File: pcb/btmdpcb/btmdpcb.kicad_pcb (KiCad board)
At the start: 2 copper layers, 60 x 25 mm, 34 parts, among them J2 ANT, T1 ED8_4, T2 ED8_4, U2 Pololu_U1V11F3, U3 LMV331

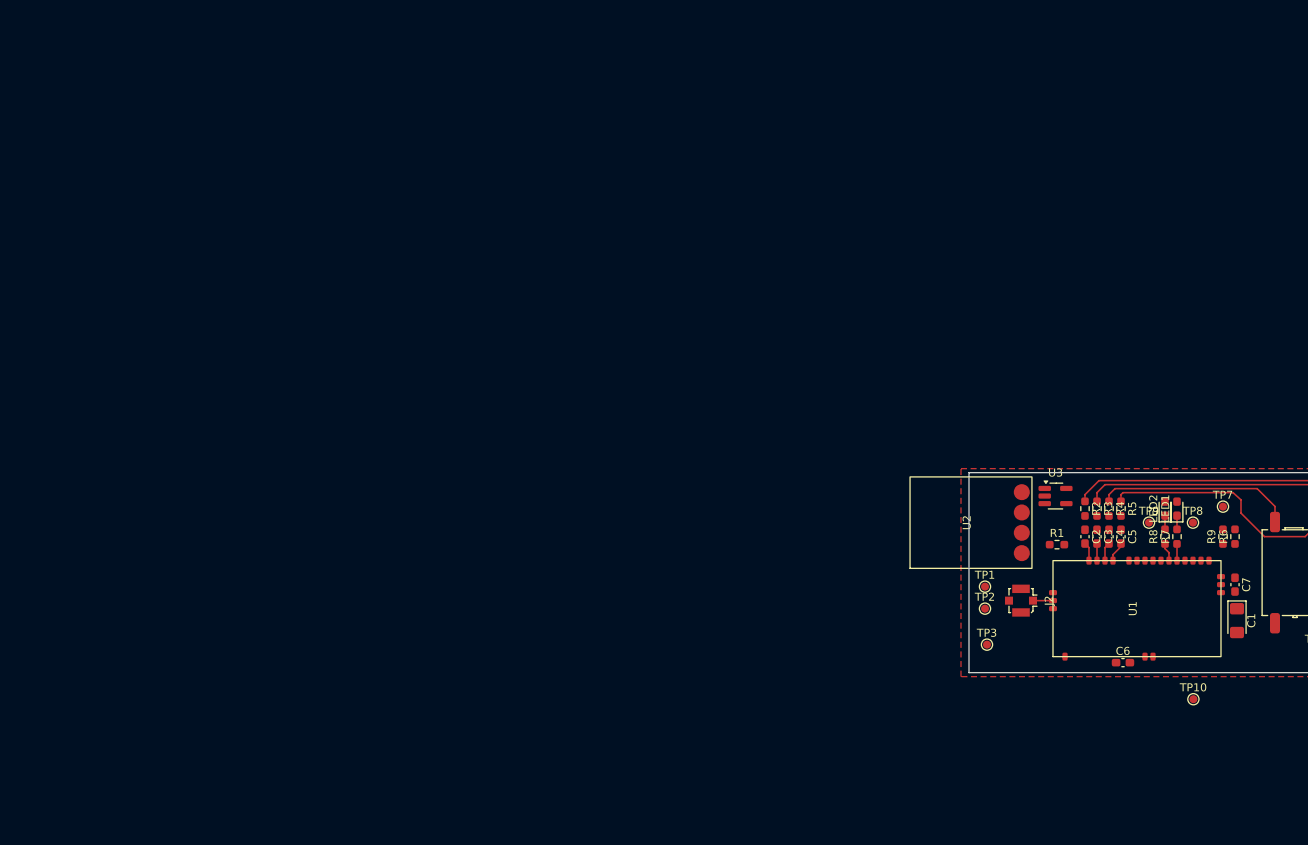
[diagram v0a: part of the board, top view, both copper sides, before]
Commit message: Update BT module symbol+footprint (correct power labels, add CE)
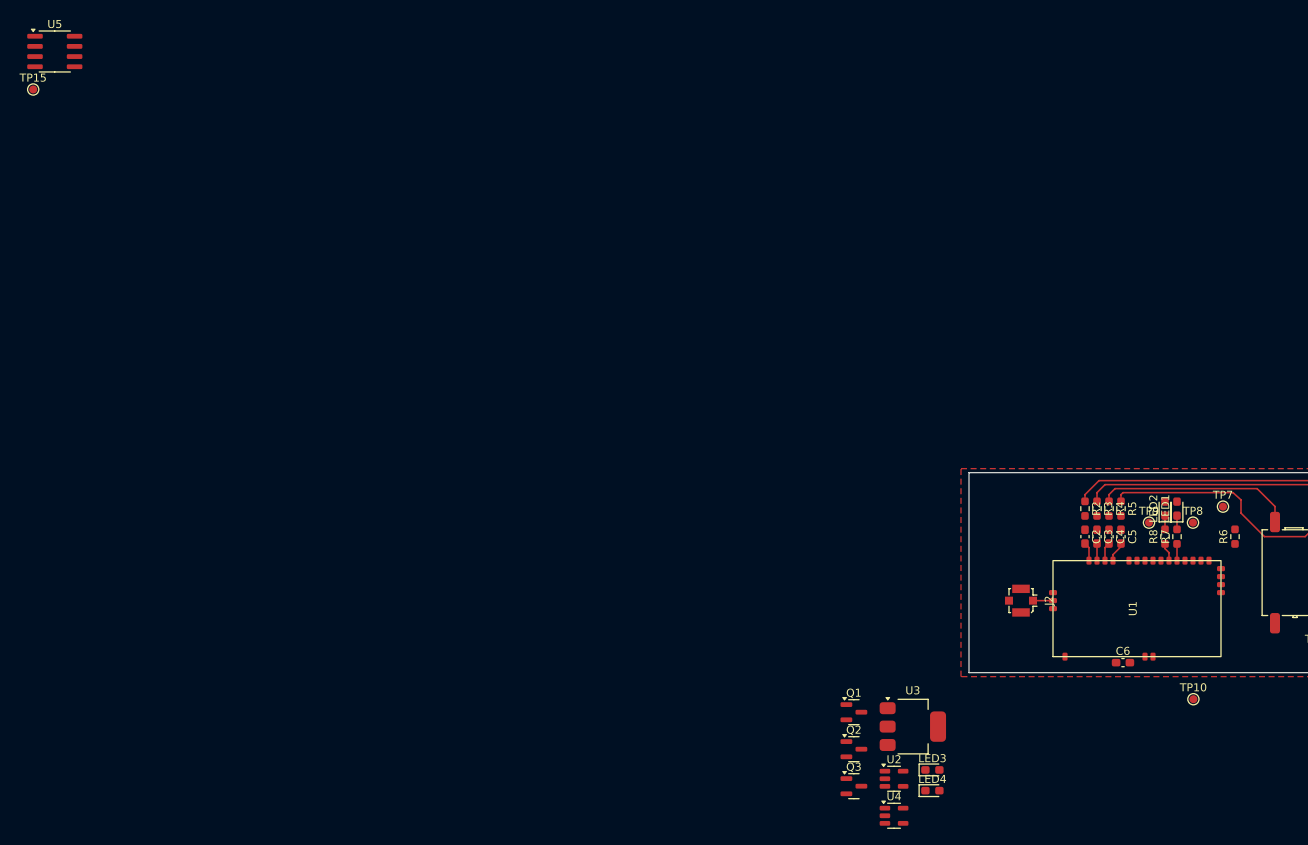
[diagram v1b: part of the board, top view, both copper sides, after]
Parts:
- removed C1: 10u, LED_SMD:LED_1206_3216Metric_Pad1.42x1.75mm_HandSolder
- removed C7: 100n, Capacitor_SMD:C_0603_1608Metric_Pad1.08x0.95mm_HandSolder
- removed R1: 10k, Resistor_SMD:R_0603_1608Metric_Pad0.98x0.95mm_HandSolder
- removed R9: 1k, Resistor_SMD:R_0603_1608Metric_Pad0.98x0.95mm_HandSolder
- removed TP1: BAT+, TestPoint:TestPoint_Pad_D1.0mm
- removed TP2: BAT-, TestPoint:TestPoint_Pad_D1.0mm
- removed TP3: ~{SHDN}, TestPoint:TestPoint_Pad_D1.0mm
- added LED3: RD, LED_SMD:LED_0603_1608Metric_Pad1.05x0.95mm_HandSolder, F.Cu at (113.4, 92.7)
- added LED4: GN, LED_SMD:LED_0603_1608Metric_Pad1.05x0.95mm_HandSolder, F.Cu at (113.4, 95.2)
- added Q1: AO3401A, Package_TO_SOT_SMD:SOT-23, F.Cu at (103.6, 85.4)
- added Q2: AO3401A, Package_TO_SOT_SMD:SOT-23, F.Cu at (103.6, 90.1)
- added Q3: MMBT3904, Package_TO_SOT_SMD:SOT-23, F.Cu at (103.6, 94.7)
- added TP15: TestPoint, TestPoint:TestPoint_Pad_D1.0mm, F.Cu at (1.02, 7.61)
- added U4: TP4057, Package_TO_SOT_SMD:TSOT-23-5, F.Cu at (108.6, 98.4)
- added U5: MC34063AD, Package_SO:SOIC-8_3.9x4.9mm_P1.27mm, F.Cu at (3.73, 2.85)
- U2: value Pololu_U1V11F3 -> ME6211C33M5; footprint modules:Pololu_U1V11F3 -> Package_TO_SOT_SMD:SOT-23-5
- U3: value LMV331 -> AMS1117-1.5; footprint Package_TO_SOT_SMD:SOT-23-5_HandSoldering -> Package_TO_SOT_SMD:SOT-223-3_TabPin2
- moved U3 33.9 mm to (111.0, 87.2)
- moved U2 33.4 mm to (108.6, 93.8), turned to 0 degrees
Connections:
- C6 pad 1: +3.3V -> +3V3
- LED1 pad 2: +3.3V -> +3V3
- LED2 pad 2: +3.3V -> +3V3
- TP10 pad 1: Net-(U1-D1) -> Net-(U1-BAT+)
- U1 pad 11: +3.3V -> +3V3
- U1 pad 29: +3.3V -> Net-(U1-BAT+)
- U1 pad 31: Net-(U1-D1) -> unconnected-(U1-D1-Pad31)
- U2 pad 1: Net-(U2-~{SHDN}) -> VCC
- U2 pad 2: +BATT -> GND
- U2 pad 3: GND -> Net-(U2-CE)
- U2 pad 4: +3.3V -> unconnected-(U2-NC-Pad4)
- U3 pad 1: unconnected-(U3-+-Pad1) -> GND
- U3 pad 2: GND -> +1V5
- U3 pad 3: unconnected-(U3---Pad3) -> Net-(Q2-D)

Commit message: [WIP] Design eval board for all relevant functions
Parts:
- removed C6: 100n, Capacitor_SMD:C_0603_1608Metric_Pad1.08x0.95mm_HandSolder
- removed R7: 100R, Resistor_SMD:R_0603_1608Metric_Pad0.98x0.95mm_HandSolder
- removed TP15: TestPoint, TestPoint:TestPoint_Pad_D1.0mm
- removed U3: AMS1117-1.5, Package_TO_SOT_SMD:SOT-223-3_TabPin2
- removed U5: MC34063AD, Package_SO:SOIC-8_3.9x4.9mm_P1.27mm
- added C1: 1u, Capacitor_SMD:C_0603_1608Metric_Pad1.08x0.95mm_HandSolder, F.Cu at (215.3, 73.7)
- added C1in1: 100u, Capacitor_SMD:C_Elec_6.3x7.7, F.Cu at (208.8, 93.6)
- added C1out1: 22u, Capacitor_SMD:C_Elec_6.3x5.4, F.Cu at (208.8, 101.7)
- added C2in1: 22u, Capacitor_SMD:C_Elec_6.3x5.4, F.Cu at (228.8, 93.6)
- added C2out1: 22u, Capacitor_SMD:C_Elec_6.3x5.4, F.Cu at (228.8, 101.7)
- added C3ff1: 22p, Capacitor_SMD:C_0603_1608Metric_Pad1.08x0.95mm_HandSolder, F.Cu at (241.2, 74.1)
- added C3in1: 10u, Capacitor_SMD:C_0805_2012Metric_Pad1.18x1.45mm_HandSolder, F.Cu at (236.6, 68.4)
- added C3out1: 10u, Capacitor_SMD:C_0805_2012Metric_Pad1.18x1.45mm_HandSolder, F.Cu at (236.6, 71.4)
- added Ct1: 270p, Capacitor_SMD:C_0805_2012Metric_Pad1.18x1.45mm_HandSolder, F.Cu at (216.2, 95.5)
- added Ct2: 245p, Capacitor_SMD:C_0805_2012Metric_Pad1.18x1.45mm_HandSolder, F.Cu at (236.2, 104.5)
- added D2: 1N5819, Diode_SMD:D_SMA, F.Cu at (217.8, 91.8)
- added Q4: AO3401A, Package_TO_SOT_SMD:SOT-23, F.Cu at (243.4, 91.9)
- added Q5: AO3401A, Package_TO_SOT_SMD:SOT-23, F.Cu at (243.4, 96.5)
- added Q6: BSD235C, Package_TO_SOT_SMD:SOT-363_SC-70-6, F.Cu at (258.0, 73.3)
- added R18: 1.5, Resistor_SMD:R_0805_2012Metric_Pad1.20x1.40mm_HandSolder, F.Cu at (201.5, 91.0)
- added R19: 7k5, Resistor_SMD:R_0805_2012Metric_Pad1.20x1.40mm_HandSolder, F.Cu at (201.5, 93.9)
- added R1sc1: 0R2, Resistor_SMD:R_0805_2012Metric_Pad1.20x1.40mm_HandSolder, F.Cu at (201.5, 96.9)
- added R1sc2: 0R2, Resistor_SMD:R_0805_2012Metric_Pad1.20x1.40mm_HandSolder, F.Cu at (201.5, 99.8)
- added R1sc3: 0R2, Resistor_SMD:R_0805_2012Metric_Pad1.20x1.40mm_HandSolder, F.Cu at (201.5, 102.8)
- added R1sc4: 0R2, Resistor_SMD:R_0805_2012Metric_Pad1.20x1.40mm_HandSolder, F.Cu at (201.5, 105.7)
- added R1sc5: 0R2, Resistor_SMD:R_0805_2012Metric_Pad1.20x1.40mm_HandSolder, F.Cu at (201.5, 108.7)
- added R20: 225k, Resistor_SMD:R_0805_2012Metric_Pad1.20x1.40mm_HandSolder, F.Cu at (236.2, 91.0)
- added R21: 150k, Resistor_SMD:R_0805_2012Metric_Pad1.20x1.40mm_HandSolder, F.Cu at (236.2, 93.9)
- added R2pg1: 100k, Resistor_SMD:R_0805_2012Metric_Pad1.20x1.40mm_HandSolder, F.Cu at (236.2, 96.9)
- added R3fbb1: 115k, Resistor_SMD:R_0805_2012Metric_Pad1.20x1.40mm_HandSolder, F.Cu at (241.4, 68.4)
- added R3fbt1: 100k, Resistor_SMD:R_0805_2012Metric_Pad1.20x1.40mm_HandSolder, F.Cu at (241.4, 71.3)
- added TP3: TestPoint, TestPoint:TestPoint_Pad_D1.0mm, F.Cu at (256.5, 82.3)
- added U6: MC34063AD, Package_SO:SOIC-8_3.9x4.9mm_P1.27mm, F.Cu at (208.1, 109.2)
- added U7: AP3402, Package_TO_SOT_SMD:TSOT-23-6, F.Cu at (236.4, 100.7)
- C5: value 1u -> 100n
- LED3: value RD -> GN
- LED4: value GN -> RD
- Q3: value MMBT3904 -> BSS138
- R6: value 10k -> 100R
- TP10: value TestPoint -> LED2
- TP4: value L_IN -> TestPoint
- TP5: value AUDIO_GND -> TestPoint
- TP6: value R_IN -> TestPoint
- TP7: value BTN -> TestPoint
- TP8: value LED1 -> TestPoint
- TP9: value LED2 -> LED1
- U1: footprint modules:BT -> bt_audio:bt_audio_smd
- moved Q3 154.2 mm to (255.1, 65.9)
- moved Q1 139.3 mm to (241.0, 62.7)
- moved U4 138.5 mm to (241.1, 58.1)
- moved U2 128.9 mm to (236.8, 79.7)
- moved LED3 128.0 mm to (236.4, 57.0)
- moved LED4 128.0 mm to (236.4, 59.6)
- moved TP5 107.5 mm to (271.3, 84.8)
- moved J2 103.4 mm to (227.9, 75.5), turned to 0 degrees
- moved TP6 100.7 mm to (261.1, 65.0)
- moved TP4 100.4 mm to (271.3, 81.8)
- moved LED2 87.5 mm to (227.0, 82.4), turned to 0 degrees
- moved R2 86.8 mm to (215.3, 86.2), turned to 0 degrees
- moved R3 86.7 mm to (219.6, 73.7), turned to 0 degrees
- moved R4 85.6 mm to (219.6, 76.2), turned to 0 degrees
- moved LED1 85.4 mm to (227.0, 79.8), turned to 0 degrees
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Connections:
- net Net-(U2-CE) renamed /power_3v3/EN
- C2 pad 2: Net-(U1-L+) -> Net-(U1-L-)
- C3 pad 2: Net-(U1-L-) -> Net-(U1-R-)
- C4 pad 2: Net-(U1-R-) -> Net-(U1-R+)
- C5 pad 1: Net-(C5-Pad1) -> +3V3
- C5 pad 2: Net-(U1-R+) -> GND
- LED3 pad 2: unconnected-(LED3-A-Pad2) -> Net-(LED3-A)
- Q1 pad 2: VCC -> /supply/Vsupply
- Q2 pad 1: Net-(Q2-G) -> /EN_1V5
- Q2 pad 2: VCC -> +BATT
- Q2 pad 3: Net-(Q2-D) -> EN_1V5
- R2 pad 2: Net-(C2-Pad1) -> Net-(C1-Pad1)
- R3 pad 2: Net-(C3-Pad1) -> Net-(C2-Pad1)
- R4 pad 2: Net-(C4-Pad1) -> Net-(C3-Pad1)
- R5 pad 2: Net-(C5-Pad1) -> Net-(C4-Pad1)
- R6 pad 1: Net-(U1-BTN) -> Net-(U1-LED1)
- R6 pad 2: Net-(BTN1-Pad1) -> Net-(LED1-K)
- T1 pad 1: Net-(T1-Pad1) -> /MD unit/AUDIO_L
- T1 pad 2: Net-(T1-Pad2) -> /MD unit/AUDIO_GND
- T2 pad 1: Net-(T2-Pad1) -> /MD unit/AUDIO_R
- T2 pad 2: Net-(T1-Pad2) -> /MD unit/AUDIO_GND
- TP10 pad 1: Net-(U1-BAT+) -> Net-(LED2-K)
- TP4 pad 1: Net-(T1-Pad1) -> /MD unit/~{BTN_REC}
- TP5 pad 1: Net-(T1-Pad2) -> +2V5
- TP6 pad 1: Net-(T2-Pad1) -> /MD unit/~{BTN_PAUSE}
- TP7 pad 1: Net-(BTN1-Pad1) -> Net-(U1-BAT+)
- TP8 pad 1: Net-(LED1-K) -> /bt_module/PWR_EN
- TP9 pad 1: Net-(LED2-K) -> Net-(LED1-K)
- U1 pad 28: Net-(U1-BTN) -> /bt_module/BTN
- U1 pad 30: (no net) -> /bt_module/PWR_EN
- U2 pad 1: VCC -> /power_3v3/Vin
- U4 pad 1: Net-(LED3-K) -> Net-(LED4-K)
- U4 pad 5: Net-(LED4-K) -> Net-(LED3-K)
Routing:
- net /MD unit/~{SW_HOLD}: track 0.00 -> 115.3 mm
- net +2V5: track 0.00 -> 65.0 mm
- net /MD unit/~{BTN_REC}: track 0.00 -> 42.5 mm
- net (no net): track 0.00 -> 3.90 mm

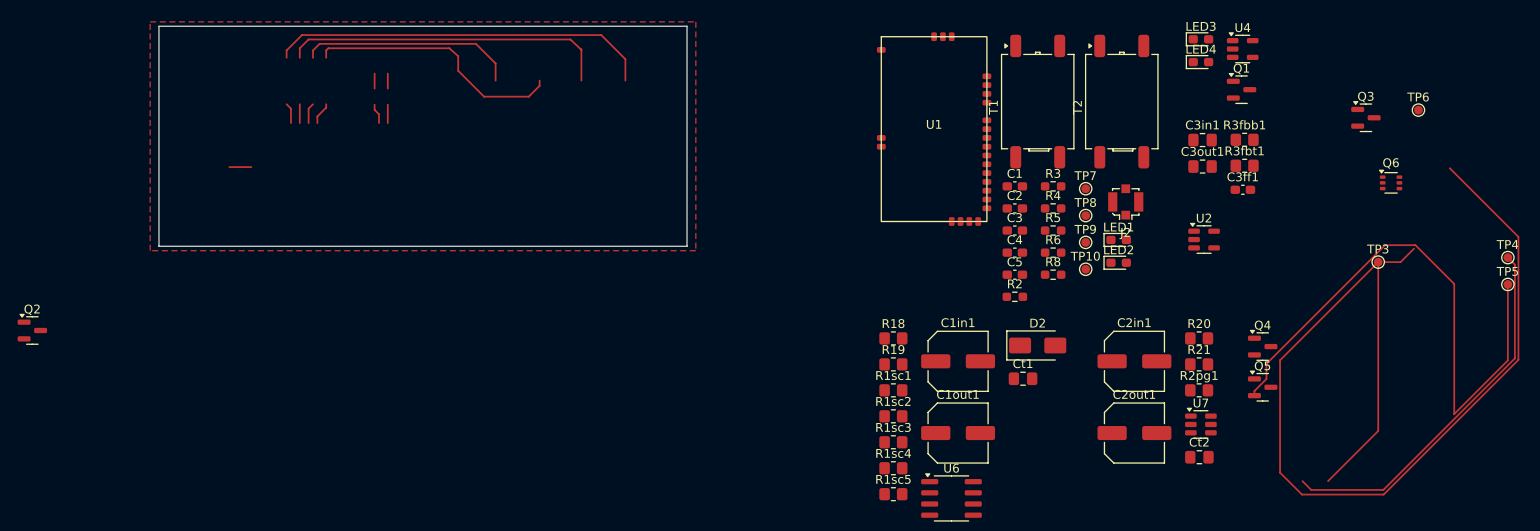
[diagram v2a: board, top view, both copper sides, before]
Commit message: Clean up schematic, implement all logic functionality
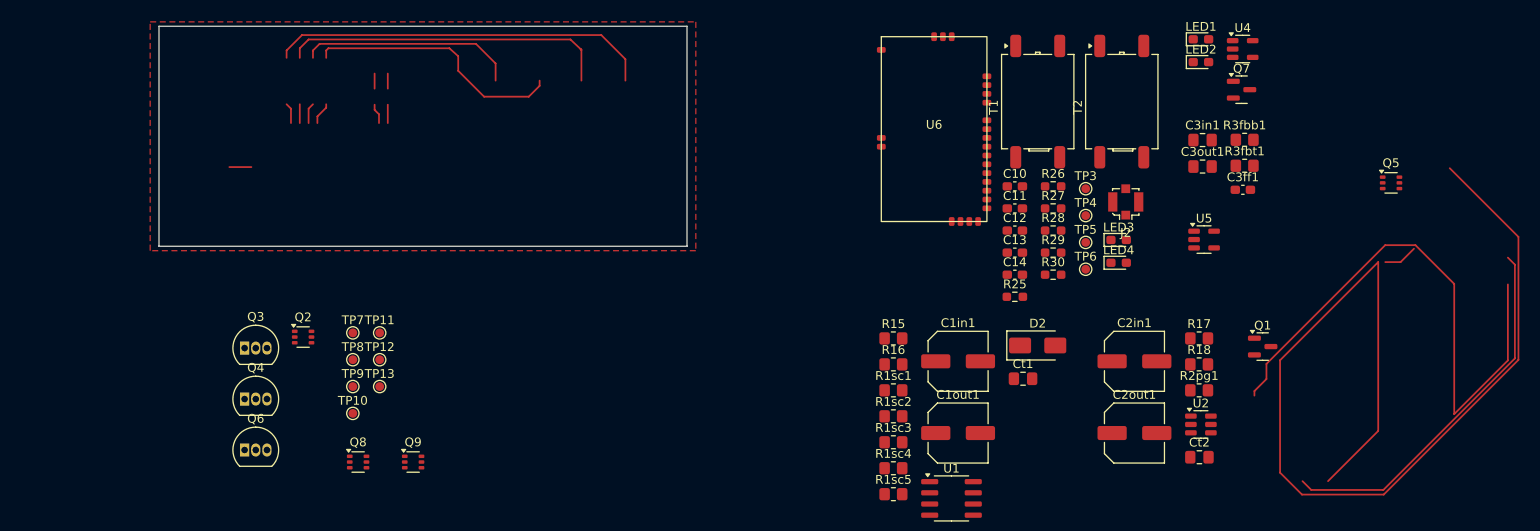
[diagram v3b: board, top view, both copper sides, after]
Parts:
- removed the Q5 at (243.4, 96.5)
- removed the TP3 at (256.5, 82.3)
- removed the TP4 at (271.3, 81.8)
- removed the TP5 at (271.3, 84.8)
- removed the TP6 at (261.1, 65.0)
- added Q4: 2N7000, Package_TO_SOT_THT:TO-92_Inline, F.Cu at (127.7, 97.9)
- added Q6: 2N7000, Package_TO_SOT_THT:TO-92_Inline, F.Cu at (127.7, 103.6)
- added Q8: BSD235C, Package_TO_SOT_SMD:SOT-363_SC-70-6, F.Cu at (140.6, 105.0)
- added Q9: BSD235C, Package_TO_SOT_SMD:SOT-363_SC-70-6, F.Cu at (146.9, 105.0)
- added TP10: TestPoint, TestPoint:TestPoint_Pad_D1.0mm, F.Cu at (140.0, 99.5)
- added TP11: TestPoint, TestPoint:TestPoint_Pad_D1.0mm, F.Cu at (143.1, 90.3)
- added TP12: TestPoint, TestPoint:TestPoint_Pad_D1.0mm, F.Cu at (143.1, 93.4)
- added TP13: TestPoint, TestPoint:TestPoint_Pad_D1.0mm, F.Cu at (143.1, 96.4)
- added TP7: TestPoint, TestPoint:TestPoint_Pad_D1.0mm, F.Cu at (140.0, 90.3)
- added TP8: TestPoint, TestPoint:TestPoint_Pad_D1.0mm, F.Cu at (140.0, 93.4)
- added TP9: TestPoint, TestPoint:TestPoint_Pad_D1.0mm, F.Cu at (140.0, 96.4)
- Q2: value AO3401A -> BSD235C; footprint Package_TO_SOT_SMD:SOT-23 -> Package_TO_SOT_SMD:SOT-363_SC-70-6
- Q3: value BSS138 -> 2N7000; footprint Package_TO_SOT_SMD:SOT-23 -> Package_TO_SOT_THT:TO-92_Inline
- moved Q3 130.1 mm to (127.7, 92.1)
- moved Q2 30.8 mm to (134.4, 90.8)
- renumbered C1 to C10, C2 to C11, C3 to C12, C4 to C13, C5 to C14, LED3 to LED1, LED4 to LED2, LED1 to LED3, LED2 to LED4, Q4 to Q1, Q6 to Q5, Q1 to Q7, R18 to R15, R19 to R16, R20 to R17, R21 to R18, R2 to R25, R3 to R26, R4 to R27, R5 to R28, R6 to R29, R8 to R30, TP7 to TP3, TP8 to TP4, TP9 to TP5, TP10 to TP6, U6 to U1, U7 to U2, U2 to U5, U1 to U6
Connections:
- net /MD unit/AUDIO_GND renamed /MD unit (MZ-N505)/AUDIO_GND
- net /MD unit/AUDIO_L renamed /MD unit (MZ-N505)/AUDIO_L
- net /MD unit/AUDIO_R renamed /MD unit (MZ-N505)/AUDIO_R
- net Net-(D1-A) renamed VBUS
- Q1 pad 1: /EN_1V5 -> ~{EN_1V5}
- Q2 pad 1: /EN_1V5 -> GND
- Q2 pad 2: +BATT -> /HOLD
- Q2 pad 3: EN_1V5 -> Net-(Q2B-DP)
- Q3 pad 1: Net-(Q3-G) -> GND
- Q3 pad 2: GND -> /HOLD
- Q5 pad 1: unconnected-(Q6A-SN-Pad1) -> GND
- Q5 pad 2: unconnected-(Q6A-GN-Pad2) -> VDD
- Q5 pad 3: unconnected-(Q6B-DP-Pad3) -> EN_1V5
- Q5 pad 4: unconnected-(Q6B-SP-Pad4) -> +BATT
- Q5 pad 5: unconnected-(Q6B-GP-Pad5) -> ~{EN_1V5}
- Q5 pad 6: unconnected-(Q6A-DN-Pad6) -> ~{EN_1V5}
- Q7 pad 2: /supply/Vsupply -> +BATT
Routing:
- net (no net): track 3.90 -> 375.9 mm
- net /MD unit/~{SW_HOLD}: track 115.3 -> 0.00 mm
- net +2V5: track 65.0 -> 0.00 mm
- net Net-(R25-Pad1): track 43.6 -> 0.00 mm
- net /MD unit/~{BTN_REC}: track 42.5 -> 0.00 mm
- net Net-(R26-Pad1): track 37.6 -> 0.00 mm
- net Net-(R28-Pad1): track 29.5 -> 0.00 mm
- net Net-(R27-Pad1): track 24.8 -> 0.00 mm
- net Net-(U6-R+): track 2.55 -> 0.00 mm
- net Net-(U6-R-): track 2.34 -> 0.00 mm
- net Net-(U6-L+): track 2.34 -> 0.00 mm
- net Net-(U6-LED2): track 2.29 -> 0.00 mm
- net Net-(U6-L-): track 2.14 -> 0.00 mm
- net Net-(U6-LED1): track 2.09 -> 0.00 mm
- net Net-(LED4-K): track 1.71 -> 0.00 mm
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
